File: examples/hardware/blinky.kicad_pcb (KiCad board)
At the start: 2 copper layers, 40 x 20 mm, 2 parts

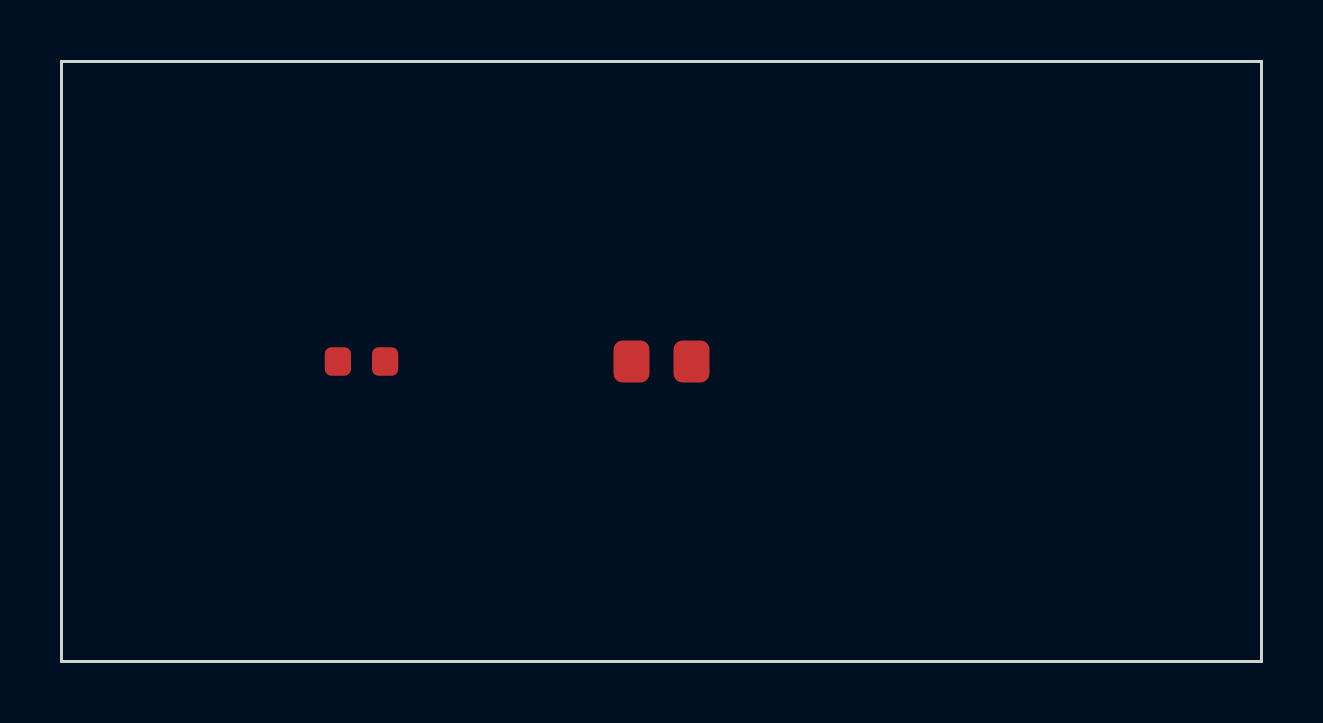
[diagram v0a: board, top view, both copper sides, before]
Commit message: fix(kicad): KiCad 9 compat — net_class design rules, pad at/size, stroke outline syntax
Co-Authored-By: Claude Fable 5 <noreply@anthropic.com>
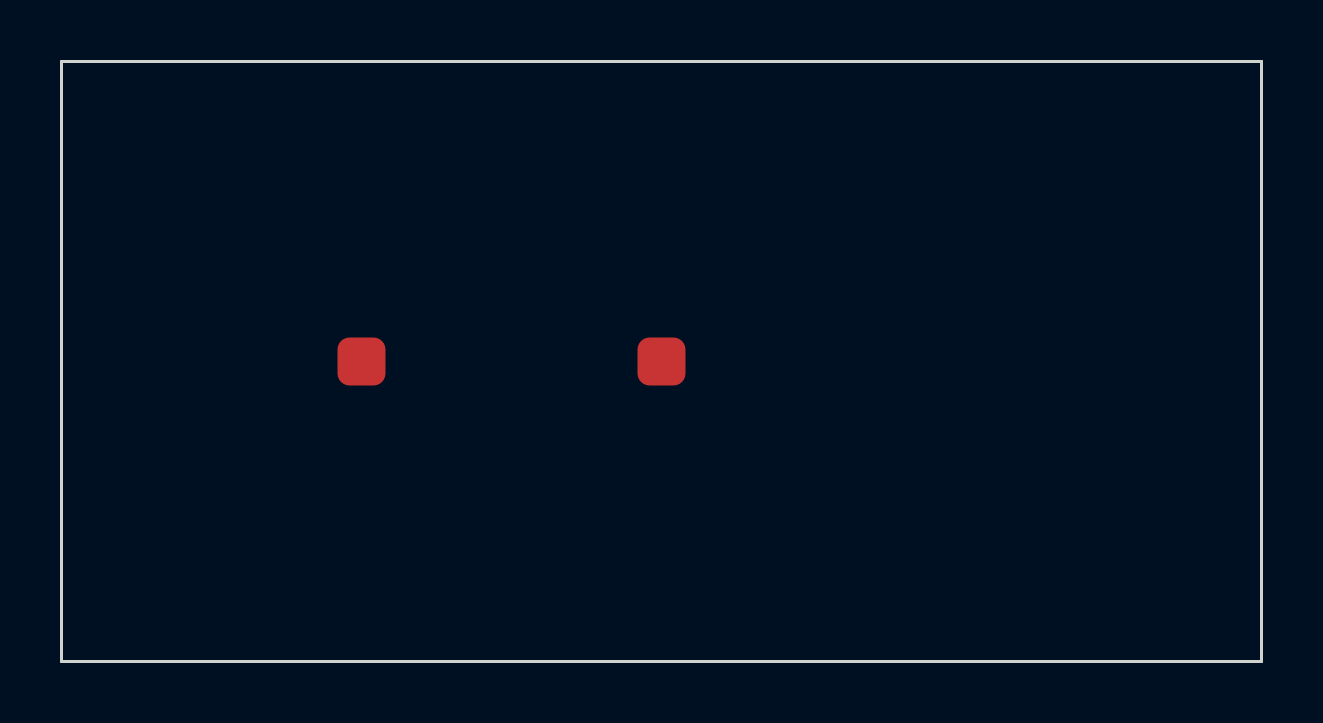
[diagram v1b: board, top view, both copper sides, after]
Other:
- net class Default added: clearance 0.2, trace_width 0.25, via_dia 0.8, via_drill 0.4
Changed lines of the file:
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@@
-(kicad_pcb (version 20221018) (generator pcbnew)
-  (general (thickness 1.6))
-  (paper "A4")
-  (layers
-    (0 "F.Cu" signal)
-    (31 "B.Cu" signal)
-    (44 "Edge.Cuts" user)
-  )
-  (setup
-    (pad_to_mask_clearance 0)
-    (clearance 0.2)
-    (trace_width 0.25)
-    (via_diameter 0.8)
-    (via_drill 0.4)
-  )
-  (net 0 "")
-  (net 1 "GND")
-  (net 2 "+3V3")
-  (net 3 "LED_A")
-  (footprint "Resistor_SMD:R_0603_1608Metric" (layer "F.Cu")
-    (at 100 50 0)
-    (property "Reference" "R1")
-    (property "Value" "330R")
-    (pad "1" smd roundrect (at -0.7875 0 0) (size 0.875 0.95) (layers "F.Cu") (net 2 "+3V3"))
-    (pad "2" smd roundrect (at 0.7875 0 0) (size 0.875 0.95) (layers "F.Cu") (net 3 "LED_A"))
-  )
-  (footprint "LED_SMD:LED_0805_2012Metric" (layer "F.Cu")
-    (at 110 50 0)
-    (property "Reference" "D1")
-    (property "Value" "RED")
-    (pad "1" smd roundrect (at -1 0 0) (size 1.2 1.4) (layers "F.Cu") (net 3 "LED_A"))
-    (pad "2" smd roundrect (at 1 0 0) (size 1.2 1.4) (layers "F.Cu") (net 1 "GND"))
-  )
-  (gr_line (start 90 40) (end 130 40) (layer "Edge.Cuts") (width 0.1))
-  (gr_line (start 130 40) (end 130 60) (layer "Edge.Cuts") (width 0.1))
-  (gr_line (start 130 60) (end 90 60) (layer "Edge.Cuts") (width 0.1))
-  (gr_line (start 90 60) (end 90 40) (layer "Edge.Cuts") (width 0.1))
-)
+(kicad_pcb (version 20240108) (generator pcbnew) (general (thickness 1.6)) (paper "A4") (layers (0 F.Cu signal) (31 B.Cu signal) (44 Edge.Cuts user)) (setup (pad_to_mask_clearance 0)) (net 0 "") (net 1 "GND") (net 2 "+3V3") (net 3 "LED_A") (net_class "Default" "ForgeLab default net class" (clearance 0.2) (trace_width 0.25) (via_dia 0.8) (via_drill 0.4) (add_net "GND") (add_net "+3V3") (add_net "LED_A")) (footprint "Resistor_SMD:R_0603_1608Metric" (layer "F.Cu") (at 100 50 0) (property "Reference" "R1") (property "Value" "330R") (pad "1" smd roundrect (at 0 0) (size 1.6 1.6) (layers "F.Cu") (net 2 "+3V3")) (pad "2" smd roundrect (at 0 0) (size 1.6 1.6) (layers "F.Cu") (net 3 "LED_A"))) (footprint "LED_SMD:LED_0805_2012Metric" (layer "F.Cu") (at 110 50 0) (property "Reference" "D1") (property "Value" "RED") (pad "1" smd roundrect (at 0 0) (size 1.6 1.6) (layers "F.Cu") (net 3 "LED_A")) (pad "2" smd roundrect (at 0 0) (size 1.6 1.6) (layers "F.Cu") (net 1 "GND"))) (gr_line (start 90 40) (end 130 40) (stroke (width 0.1) (type solid)) (layer "Edge.Cuts")) (gr_line (start 130 40) (end 130 60) (stroke (width 0.1) (type solid)) (layer "Edge.Cuts")) (gr_line (start 130 60) (end 90 60) (stroke (width 0.1) (type solid)) (layer "Edge.Cuts")) (gr_line (start 90 60) (end 90 40) (stroke (width 0.1) (type solid)) (layer "Edge.Cuts")))
